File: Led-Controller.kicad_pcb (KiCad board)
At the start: 2 copper layers, 71.3 x 47.1 mm, 72 parts, among them J1 Program, J2 Barrel_Jack, J3 Screw_Terminal, Q1 CSD18540Q5B, Q2 CSD18540Q5B, Q3 CSD18540Q5B, Q4 CSD18540Q5B, Q5 CSD18540Q5B, Q6 CSD18540Q5B, U1 TPS5430DDA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

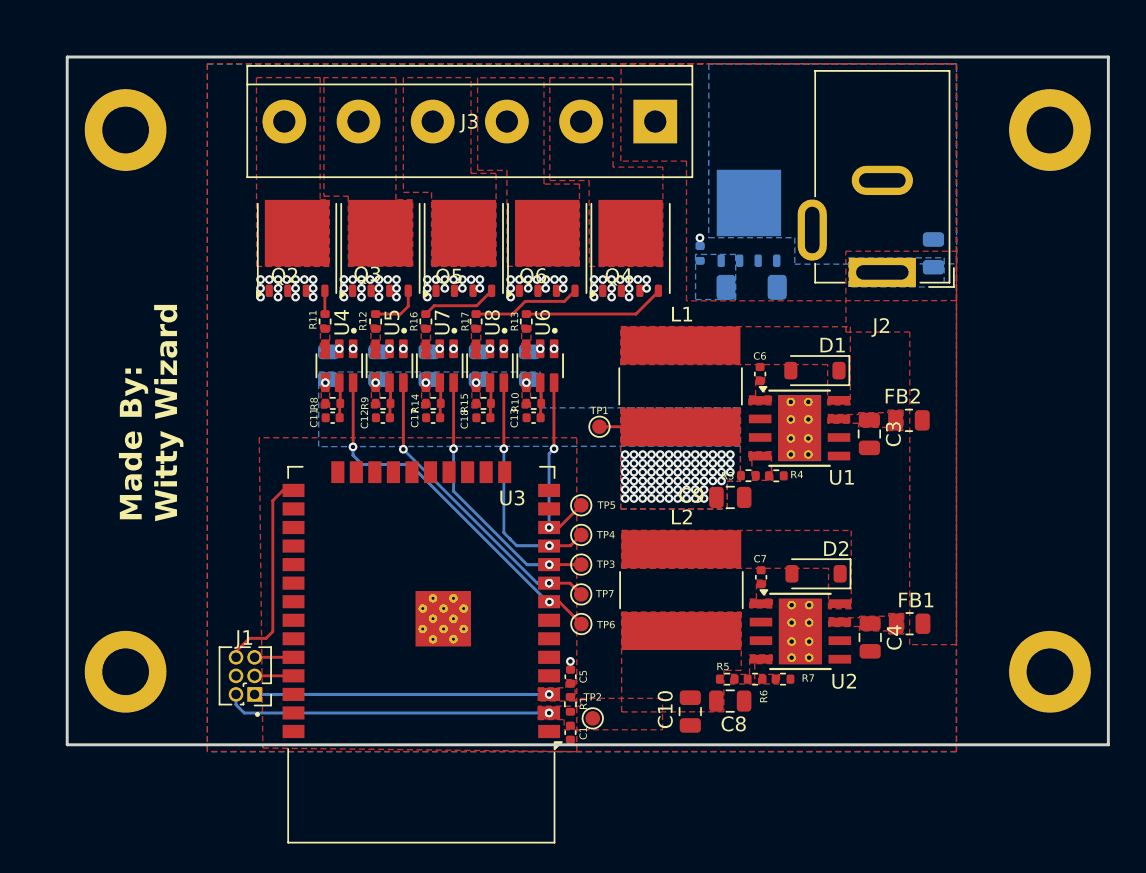
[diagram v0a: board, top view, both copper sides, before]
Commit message: Added: New power stage
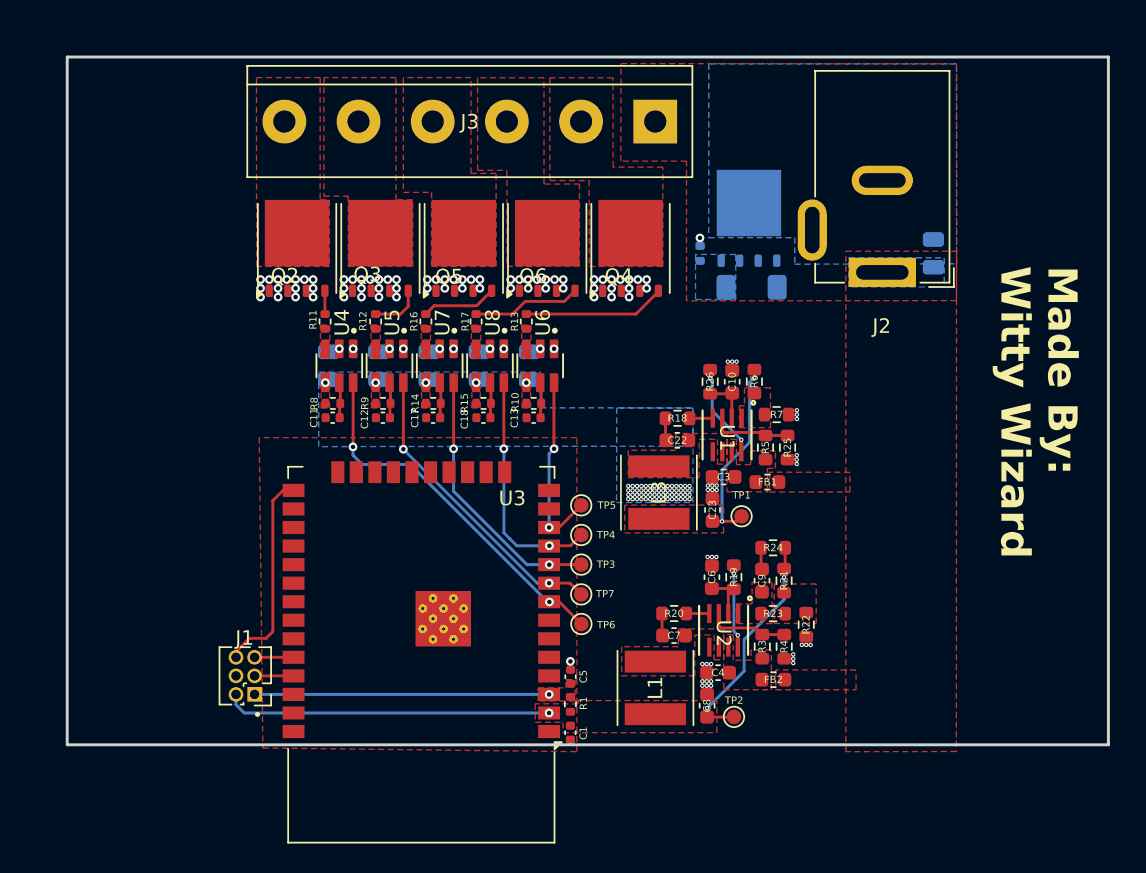
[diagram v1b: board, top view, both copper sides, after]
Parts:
- removed D1, D2: DSK34, Diode_SMD:D_SOD-123
- removed L2: 15uH, Inductor_SMD:L_Bourns-SRN8040_8x8.15mm
- removed REF** (x4): MountingHole_3.2mm_M3_DIN965_Pad, MountingHole:MountingHole_3.2mm_M3_DIN965_Pad
- added C22: 100n, Capacitor_SMD:C_0603_1608Metric, F.Cu at (145.7, 86.2)
- added C23: 33u, Capacitor_SMD:C_0603_1608Metric, F.Cu at (148.1, 91.0)
- added L3: 10u, Inductor_SMD:L_Taiyo-Yuden_MD-5050, F.Cu at (144.4, 89.8)
- added R18: 20, Resistor_SMD:R_0603_1608Metric, F.Cu at (145.7, 84.7)
- added R19: 100k, Resistor_SMD:R_0603_1608Metric, F.Cu at (149.6, 95.6)
- added R20: 20, Resistor_SMD:R_0603_1608Metric, F.Cu at (145.5, 98.1)
- added R21: 243k, Resistor_SMD:R_0603_1608Metric, F.Cu at (153.0, 95.8)
- added R22: 76.8k, Resistor_SMD:R_0603_1608Metric, F.Cu at (154.5, 98.8)
- added R23: 487, Resistor_SMD:R_0603_1608Metric, F.Cu at (152.2, 98.1)
- added R24: 243k, Resistor_SMD:R_0603_1608Metric, F.Cu at (152.2, 93.6)
- added R25: 21k, Resistor_SMD:R_0603_1608Metric, F.Cu at (153.2, 86.7)
- added R26: 100k, Resistor_SMD:R_0603_1608Metric, F.Cu at (147.9, 82.2)
- C10: value 22uf -> 100n; footprint Capacitor_SMD:C_0805_2012Metric -> Capacitor_SMD:C_0603_1608Metric
- C3, C4, C8: value 22uf -> 33u; footprint Capacitor_SMD:C_0805_2012Metric -> Capacitor_SMD:C_0603_1608Metric
- C6, C7: value 10nf -> 100n; footprint Capacitor_SMD:C_0402_1005Metric -> Capacitor_SMD:C_0603_1608Metric
- C9: value 22uf -> 33p; footprint Capacitor_SMD:C_0805_2012Metric -> Capacitor_SMD:C_0603_1608Metric
- FB1, FB2: value 220Ω -> 220; footprint Resistor_SMD:R_0805_2012Metric -> Inductor_SMD:L_0603_1608Metric
- L1: value 15uH -> 10u; footprint Inductor_SMD:L_Bourns-SRN8040_8x8.15mm -> Inductor_SMD:L_Taiyo-Yuden_MD-5050
- R3, R5: value 10kΩ -> 100k; footprint Resistor_SMD:R_0402_1005Metric -> Resistor_SMD:R_0603_1608Metric
- R4: value 1.5kΩ -> 21k; footprint Resistor_SMD:R_0402_1005Metric -> Resistor_SMD:R_0603_1608Metric
- R6: value 5.6kΩ -> 41.2k; footprint Resistor_SMD:R_0402_1005Metric -> Resistor_SMD:R_0603_1608Metric
- R7: value 270Ω -> 7.68k; footprint Resistor_SMD:R_0402_1005Metric -> Resistor_SMD:R_0603_1608Metric
- U1, U2: value TPS5430DDA -> MP9943AGQ-P; footprint Package_SO:TI_SO-PowerPAD-8_ThermalVias -> MP9943A:MP9943A
- moved C10 22.8 mm to (149.4, 82.2)
- moved L1 20.7 mm to (144.2, 103.2)
- moved R6 20.4 mm to (151.0, 82.2), turned to -90 degrees
- moved FB2 20.0 mm to (152.3, 102.6)
- moved R7 18.1 mm to (152.5, 84.4)
- moved R5 16.1 mm to (151.7, 86.7), turned to 90 degrees
- moved C6 14.3 mm to (148.1, 95.6)
- moved FB1 13.7 mm to (151.8, 89.1)
- moved R3 11.7 mm to (151.5, 100.3), turned to 90 degrees
- moved R4 11.7 mm to (153.0, 100.3), turned to -90 degrees
- moved TP1 11.5 mm to (150.1, 91.4)
- moved C4 10.7 mm to (148.5, 102.1), turned to 180 degrees
- moved C3 10.4 mm to (148.8, 88.7), turned to 180 degrees
- moved TP2 9.67 mm to (149.6, 105.1)
- moved C7 7.18 mm to (145.5, 99.6), turned to 0 degrees
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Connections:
- C10 pad 1: GND -> Net-(U1-VCC)
- C10 pad 2: +3.3V -> GND
- C3 pad 1: Net-(U1-VIN) -> Net-(U1-IN)
- C4 pad 1: Net-(U2-VIN) -> Net-(U2-IN)
- C6 pad 1: Net-(U1-BOOT) -> Net-(U2-VCC)
- C6 pad 2: Net-(D1-K) -> GND
- C7 pad 1: Net-(U2-BOOT) -> Net-(C7-Pad1)
- C7 pad 2: Net-(D2-K) -> Net-(U2-SW)
- C9 pad 1: GND -> Net-(U2-FB)
- C9 pad 2: +9V -> Net-(C9-Pad2)
- FB1 pad 2: Net-(U2-VIN) -> Net-(U1-IN)
- FB2 pad 2: Net-(U1-VIN) -> Net-(U2-IN)
- L1 pad 1: Net-(D1-K) -> Net-(U2-SW)
- L1 pad 2: +9V -> +3.3V
- R3 pad 1: +9V -> Net-(U2-IN)
- R3 pad 2: Net-(U1-VSENSE) -> Net-(U2-EN/SYNC)
- R4 pad 1: Net-(U1-VSENSE) -> Net-(U2-EN/SYNC)
- R5 pad 1: +3.3V -> Net-(U1-IN)
- R5 pad 2: Net-(U2-VSENSE) -> Net-(U1-EN/SYNC)
- R6 pad 1: Net-(U2-VSENSE) -> +9V
- R6 pad 2: Net-(R6-Pad2) -> Net-(U1-FB)
- R7 pad 1: Net-(R6-Pad2) -> Net-(U1-FB)
- U1 pad 1: Net-(U1-BOOT) -> Net-(U1-FB)
- U1 pad 2: unconnected-(U1-NC-Pad2) -> Net-(U1-VCC)
- U1 pad 3: unconnected-(U1-NC-Pad3) -> Net-(U1-EN/SYNC)
- U1 pad 4: Net-(U1-VSENSE) -> Net-(U1-BST)
- U1 pad 5: unconnected-(U1-EN-Pad5) -> GND
- U1 pad 6: GND -> Net-(U1-SW)
- U1 pad 7: Net-(U1-VIN) -> Net-(U1-IN)
- U1 pad 8: Net-(D1-K) -> Net-(U1-PG)
- U2 pad 1: Net-(U2-BOOT) -> Net-(U2-FB)
- U2 pad 2: unconnected-(U2-NC-Pad2) -> Net-(U2-VCC)
- U2 pad 3: unconnected-(U2-NC-Pad3) -> Net-(U2-EN/SYNC)
- U2 pad 4: Net-(U2-VSENSE) -> Net-(U2-BST)
- U2 pad 5: unconnected-(U2-EN-Pad5) -> GND
- U2 pad 6: GND -> Net-(U2-SW)
- U2 pad 7: Net-(U2-VIN) -> Net-(U2-IN)
- U2 pad 8: Net-(D2-K) -> Net-(U2-PG)
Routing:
- net +3.3V: track 22.5 -> 38.0 mm, vias 1 -> 3
- net +9V: track 5.57 -> 12.9 mm, vias 76 -> 67
- net Net-(U1-PG): track 0.00 -> 6.50 mm, vias 0 -> 2
- net Net-(U2-PG): track 0.00 -> 5.73 mm, vias 0 -> 2
- net Net-(U1-EN/SYNC): track 0.00 -> 5.69 mm
- net Net-(U2-EN/SYNC): track 0.00 -> 5.57 mm
- net Net-(U2-VCC): track 0.00 -> 3.62 mm
- net Net-(U1-VCC): track 0.00 -> 3.26 mm
- net Net-(U1-BST): track 0.00 -> 1.59 mm
- net Net-(U2-BST): track 0.00 -> 1.59 mm
- net Net-(C7-Pad1): track 0.00 -> 1.53 mm
- net Net-(C22-Pad1): track 0.00 -> 1.53 mm
- net Net-(C9-Pad2): track 0.00 -> 1.50 mm
- net GND: vias 79 -> 110
- added copper zone on F.Cu, net Net-(R21-Pad1)
- added copper zone on F.Cu, net Net-(U1-FB)
- added copper zone on F.Cu, net Net-(U1-IN)
- added copper zone on F.Cu, net Net-(U1-SW)
- added copper zone on F.Cu, net Net-(U2-FB)
- added copper zone on F.Cu, net Net-(U2-IN)
- added copper zone on F.Cu, net Net-(U2-SW)
- removed copper zone on F.Cu, net Net-(D1-K)
- removed copper zone on F.Cu, net Net-(D2-K)
- removed copper zone on F.Cu, net Net-(R6-Pad2)
- removed copper zone on F.Cu, net Net-(U1-BOOT)
- removed copper zone on F.Cu, net Net-(U1-VIN)
- removed copper zone on F.Cu, net Net-(U1-VSENSE)
- removed copper zone on F.Cu, net Net-(U2-BOOT)
- removed copper zone on F.Cu, net Net-(U2-VIN)
- removed copper zone on F.Cu, net Net-(U2-VSENSE)

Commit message: Added: new Inductor
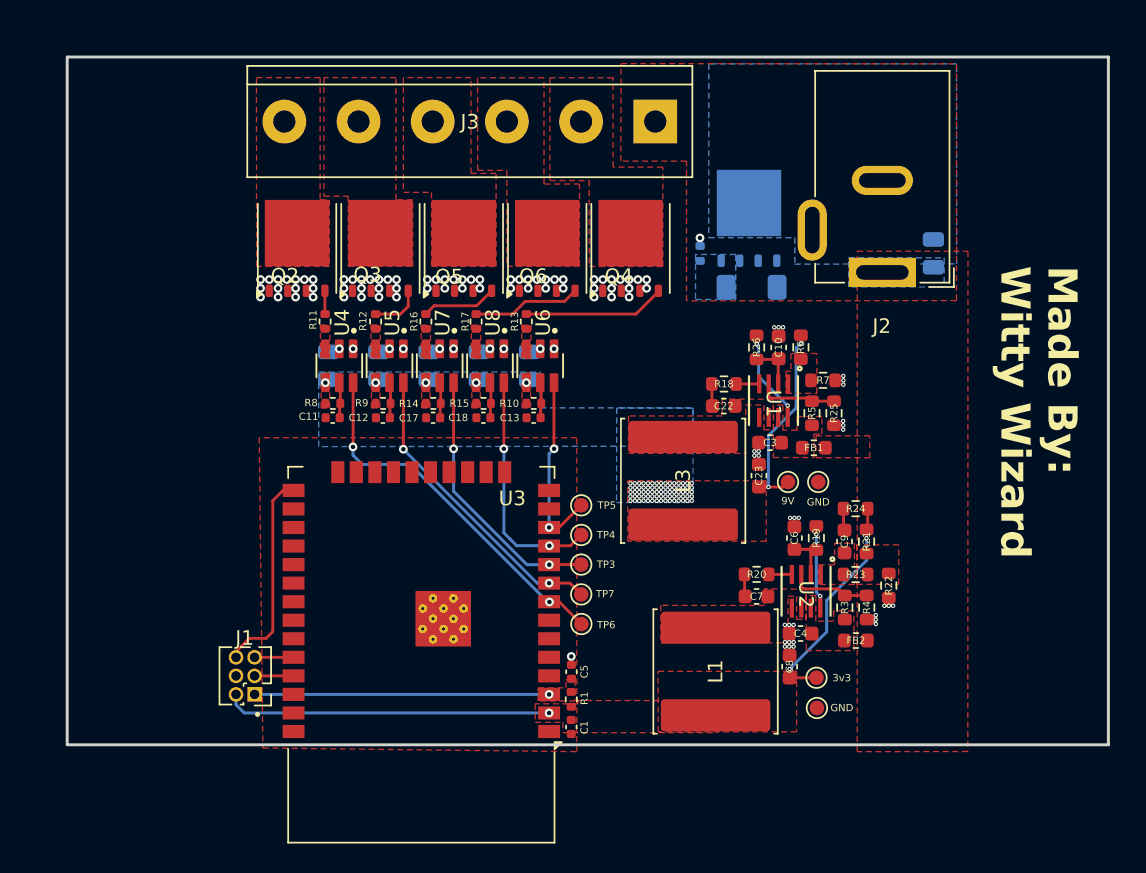
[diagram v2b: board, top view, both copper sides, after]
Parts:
- added GND: ~, TestPoint:TestPoint_Pad_D1.0mm, F.Cu at (155.2, 104.5)
- added GND: ~, TestPoint:TestPoint_Pad_D1.0mm, F.Cu at (155.3, 89.0)
- L1, L3: footprint Inductor_SMD:L_Taiyo-Yuden_MD-5050 -> Inductor_SMD:L_Changjiang_FNR8040S
- moved 3v3 6.25 mm to (155.2, 102.5)
- moved C8 6.25 mm to (153.4, 101.7)
- moved C9 6.25 mm to (157.1, 93.1)
- moved FB2 6.25 mm to (157.9, 99.9)
- moved R20 6.25 mm to (151.1, 95.4)
- moved R22 6.25 mm to (160.2, 96.1)
- moved C4 6.25 mm to (154.1, 99.4)
- moved R3 6.25 mm to (157.2, 97.7)
- moved R4 6.25 mm to (158.7, 97.7)
- moved U2 6.25 mm to (154.5, 96.5)
- moved R21 6.25 mm to (158.6, 93.1)
- moved R24 6.25 mm to (157.9, 90.9)
- moved C6 6.25 mm to (153.7, 92.9)
- moved C7 6.25 mm to (151.1, 96.9)
- moved R19 6.25 mm to (155.2, 92.9)
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- renumbered TP2 to 3v3, TP1 to 9V
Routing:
- net GND: track 0.03 -> 4.69 mm, vias 110 -> 108
- net +3.3V: track 38.0 -> 39.9 mm
- net +9V: vias 67 -> 82

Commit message: Minor fixes and layout changes
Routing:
- net +3.3V: track 39.9 -> 48.0 mm
- net +9V: track 12.9 -> 21.1 mm
- net GND: track 4.69 -> 0.35 mm
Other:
- board text added: "+VE"
- board text added: "CH1"
- board text added: "CH2"
- board text added: "CH3"
- board text added: "CH4"
- board text added: "CH5"
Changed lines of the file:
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@@
 		)
 		(property "Value" "Screw_Terminal"
-			(at 12.7 4.75 0)
+			(at 12.17 -0.04 0)
 			(layer "F.Fab")
 			(effects
@@
 		)
 		(property "Value" "Barrel_Jack"
-			(at 0 15.5 0)
+			(at -0.04 11.63 0)
 			(layer "F.Fab")
 			(effects
@@
 		)
 	)
-	(segment
-		(start 160.16 97.23)
-		(end 159.86 97.53)
-		(width 0.2)
-		(layer "F.Cu")
-		(net 1)
-	)
-	(segment
-		(start 160.16 97.23)
-		(end 160.46 97.53)
-		(width 0.2)
-		(layer "F.Cu")
-		(net 1)
-	)
-	(segment
-		(start 158.97 98.475)
-		(end 159.27 98.775)
-		(width 0.2)
-		(layer "F.Cu")
-		(net 1)
+	(gr_text "CH5\n"
+		(at 140.7 62.57 0)
+		(layer "B.SilkS")
+		(effects
+			(font
+				(size 1 1)
+				(thickness 0.25)
+				(bold yes)
+			)
+			(justify left bottom mirror)
+		)
 	)
-	(segment
-		(start 158.65 98.475)
-		(end 159.27 98.475)
-		(width 0.2)
-		(layer "F.Cu")
-		(net 1)
+	(gr_text "CH4\n"
+		(at 135.49 62.53 0)
+		(layer "B.SilkS")
+		(effects
+			(font
+				(size 1 1)
+				(thickness 0.25)
+				(bold yes)
+			)
+			(justify left bottom mirror)
+		)
 	)
-	(segment
-		(start 160.16 96.97)
-		(end 160.16 97.23)
-		(width 0.2)
-		(layer "F.Cu")
-		(net 1)
+	(gr_text "CH2"
+		(at 125.53 62.45 0)
+		(layer "B.SilkS")
+		(effects
+			(font
+				(size 1 1)
+				(thickness 0.25)
+				(bold yes)
+			)
+			(justify left bottom mirror)
+		)
 	)
-	(segment
-		(start 159.27 98.175)
-		(end 159.27 98.775)
-		(width 0.2)
-		(layer "F.Cu")
-		(net 1)
+	(gr_text "CH3\n"
+		(at 130.57 62.53 0)
+		(layer "B.SilkS")
+		(effects
+			(font
+				(size 1 1)
+				(thickness 0.25)
+				(bold yes)
+			)
+			(justify left bottom mirror)
+		)
 	)
-	(segment
-		(start 159.86 97.53)
-		(end 160.46 97.53)
-		(width 0.2)
-		(layer "F.Cu")
-		(net 1)
+	(gr_text "CH1\n"
+		(at 120.42 62.38 0)
+		(layer "B.SilkS")
+		(effects
+			(font
+				(size 1 1)
+				(thickness 0.25)
+				(bold yes)
+			)
+			(justify left bottom mirror)
+		)
 	)
-	(segment
-		(start 158.97 98.475)
-		(end 159.27 98.175)
-		(width 0.2)
-		(layer "F.Cu")
-		(net 1)
+	(gr_text "+VE"
+		(at 146.08 62.51 0)
+		(layer "B.SilkS")
+		(effects
+			(font
+				(size 1 1)
+				(thickness 0.25)
+				(bold yes)
+			)
+			(justify left bottom mirror)
+		)
 	)
 	(segment
@@
 	)
 	(segment
-		(start 160.16 96.97)
-		(end 160.16 97.53)
-		(width 0.2)
-		(layer "F.Cu")
-		(net 1)
-	)
-	(segment
 		(start 138.37 101.34)
 		(end 138.35 101.32)
@@
 	)
 	(segment
-		(start 155.91 97.16)
-		(end 155.91 99.32)
+		(start 161.4 101.59)
+		(end 161.13 101.86)
 		(width 0.2)
 		(layer "B.Cu")
@@
 	)
 	(segment
-		(start 158.64 92.9)
-		(end 158.64 94.43)
+		(start 161.13 101.86)
+		(end 153.37 101.86)
+		(width 0.2)
+		(layer "B.Cu")
+		(net 4)
+	)
+	(segment
+		(start 161.4 93.39)
+		(end 161.4 101.59)
 		(width 0.2)
 		(layer "B.Cu")
@@
 	)
 	(segment
-		(start 115.46 104.307106)
-		(end 116.022894 104.87)
+		(start 158.64 92.9)
+		(end 160.91 92.9)
 		(width 0.2)
 		(layer "B.Cu")
@@
 	)
 	(segment
-		(start 155.91 99.32)
-		(end 153.37 101.86)
+		(start 115.46 104.307106)
+		(end 116.022894 104.87)
 		(width 0.2)
 		(layer "B.Cu")
@@
 	)
 	(segment
-		(start 158.64 94.43)
-		(end 155.91 97.16)
+		(start 160.91 92.9)
+		(end 161.4 93.39)
 		(width 0.2)
 		(layer "B.Cu")
@@
 	)
 	(segment
-		(start 153.819998 83.98)
-		(end 151.919998 85.88)
+		(start 151.919998 89.4)
+		(end 157.48 89.4)
+		(width 0.2)
+		(layer "B.Cu")
+		(net 14)
+	)
+	(segment
+		(start 157.33 79.55)
+		(end 154.139998 79.55)
 		(width 0.2)
 		(layer "B.Cu")
@@
 	)
 	(segment
-		(start 153.819998 79.87)
-		(end 153.819998 83.98)
+		(start 157.8 80.02)
+		(end 157.33 79.55)
 		(width 0.2)
 		(layer "B.Cu")
@@
 	)
 	(segment
-		(start 154.139998 79.55)
-		(end 153.819998 79.87)
+		(start 157.48 89.4)
+		(end 157.8 89.08)
 		(width 0.2)
 		(layer "B.Cu")
@@
 	)
 	(segment
-		(start 151.919998 85.88)
-		(end 151.919998 89.4)
+		(start 157.8 89.08)
+		(end 157.8 80.02)
 		(width 0.2)
 		(layer "B.Cu")
@@
 		(polygon
 			(pts
-				(xy 141.83 60.4) (xy 164.8 60.42) (xy 164.8 76.63) (xy 146.31 76.65) (xy 146.31 67.08) (xy 141.81 67.08)
+				(xy 141.85 59.88) (xy 175.2 59.94) (xy 175.2 76.63) (xy 146.31 76.65) (xy 146.31 67.08) (xy 141.81 67.08)
+			)
+		)
+	)
+	(zone
+		(net 1)
+		(net_name "GND")
+		(layer "F.Cu")
+		(hatch edge 0.5)
+		(priority 24)
+		(connect_pads yes
+			(clearance 0.25)
+		)
+		(min_thickness 0.25)
+		(filled_areas_thickness no)
+		(fill yes
+			(thermal_gap 0.1)
+			(thermal_bridge_width 0.5)
+		)
+		(polygon
+			(pts
+				(xy 158.17 98.02) (xy 158.17 98.93) (xy 160.64 98.93) (xy 160.64 96.55) (xy 159.63 96.55) (xy 159.63 98.02)
 			)
 		)
@@
 		(polygon
 			(pts
-				(xy 142.28 88.97) (xy 151.77 88.97) (xy 151.77 93.11) (xy 142.29 93.11)
+				(xy 142.28 88.97) (xy 146.81 88.98) (xy 146.82 90.58) (xy 150.57 90.58) (xy 150.57 88.97) (xy 151.77 88.97)
+				(xy 151.77 93.11) (xy 142.29 93.11)
 			)
 		)
@@
 		(polygon
 			(pts
-				(xy 165.583222 73.249738) (xy 165.573222 107.509738) (xy 158.003222 107.519738) (xy 158.003222 73.249738)
+				(xy 175.23 73.25) (xy 175.21 107.05) (xy 158.01 107.05) (xy 158.003222 73.249738)
 			)
 		)
@@
 		(priority 1)
 		(connect_pads
-			(clearance 0.5)
+			(clearance 0.25)
 		)
 		(min_thickness 0.25)
@@
 		(fill yes
 			(thermal_gap 0.1)
-			(thermal_bridge_width 0.7)
+			(thermal_bridge_width 0.5)
 		)
 		(polygon

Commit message: Fixed DFM Issues
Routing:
- net +9V: vias 82 -> 37

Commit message: review pending
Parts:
- removed 3v3, 9V, GND (x2): ~, TestPoint:TestPoint_Pad_D1.0mm
- added C21: 470uf, Capacitor_THT:CP_Radial_D10.0mm_P2.50mm_P5.00mm, F.Cu at (164.2, 82.0)
- added C24: 470uf, Capacitor_THT:CP_Radial_D10.0mm_P2.50mm_P5.00mm, F.Cu at (166.9, 94.1)
- added C25: 100nf, Capacitor_SMD:C_0402_1005Metric, B.Cu at (108.0, 80.9)
- added C26: 100nf, Capacitor_SMD:C_0402_1005Metric, B.Cu at (111.5, 80.9)
- added C27: 100nf, Capacitor_SMD:C_0402_1005Metric, B.Cu at (114.9, 80.9)
- added C28: 100nf, Capacitor_SMD:C_0402_1005Metric, B.Cu at (118.4, 80.9)
- added C29: 100nf, Capacitor_SMD:C_0402_1005Metric, B.Cu at (121.8, 80.9)
- added C30: 100nf, Capacitor_SMD:C_0402_1005Metric, F.Cu at (134.0, 77.4)
- added C31: 22uf, Capacitor_SMD:C_0805_2012Metric, F.Cu at (135.8, 77.6)
- added C32: 100nf, Capacitor_SMD:C_0402_1005Metric, B.Cu at (106.7, 70.8)
- added C33: 100nf, Capacitor_SMD:C_0402_1005Metric, B.Cu at (111.7, 70.8)
- added C34: 100nf, Capacitor_SMD:C_0402_1005Metric, B.Cu at (116.7, 70.8)
- added C35: 100nf, Capacitor_SMD:C_0402_1005Metric, B.Cu at (121.9, 70.5)
- added C36: 100nf, Capacitor_SMD:C_0402_1005Metric, B.Cu at (127.1, 70.4)
- added J4: Screw_Terminal, TerminalBlock:TerminalBlock_bornier-2_P5.08mm, F.Cu at (167.5, 64.5)
- added J5: Ws2812 Conn, Connector_PinHeader_2.54mm:PinHeader_1x03_P2.54mm_Horizontal, F.Cu at (136.8, 70.7)
- added J6: Screw_Terminal, TerminalBlock:TerminalBlock_bornier-2_P5.08mm, F.Cu at (146.4, 64.2)
- added JP1: Jumper_3_Open, Jumper:SolderJumper-3_P2.0mm_Open_TrianglePad1.0x1.5mm, F.Cu at (143.7, 82.9)
- added R27: 100, Resistor_SMD:R_0402_1005Metric, B.Cu at (106.7, 67.9)
- added R28: 100, Resistor_SMD:R_0402_1005Metric, B.Cu at (111.8, 67.9)
- added R29: 100, Resistor_SMD:R_0402_1005Metric, B.Cu at (116.8, 67.8)
- added R30: 100, Resistor_SMD:R_0402_1005Metric, B.Cu at (121.9, 67.6)
- added R31: 100, Resistor_SMD:R_0402_1005Metric, B.Cu at (127.1, 67.3)
- added R33: 37.4k, Resistor_SMD:R_0603_1608Metric, F.Cu at (155.8, 79.9)
- added TP1: ~, TestPoint:TestPoint_Pad_D1.0mm, F.Cu at (142.7, 98.7)
- added TP2: ~, TestPoint:TestPoint_Pad_D1.0mm, F.Cu at (160.0, 104.2)
- added TP8: ~, TestPoint:TestPoint_Pad_D1.0mm, F.Cu at (115.1, 92.2)
- added U9: SN74LV1T34DBV, Package_TO_SOT_SMD:SOT-23-5, F.Cu at (139.2, 77.6)
- J1: footprint Connector_PinHeader_1.27mm:PinHeader_2x03_P1.27mm_Vertical -> Connector_PinHeader_2.54mm:PinHeader_2x03_P2.54mm_Vertical
- moved C13 12.0 mm to (123.8, 84.3)
- moved C14 12.0 mm to (116.6, 80.7)
- moved C17 12.0 mm to (116.9, 84.3)
- moved C18 12.0 mm to (120.4, 84.3)
- moved C19 12.0 mm to (120.1, 80.7)
- moved C20 12.0 mm to (123.5, 80.7)
- moved Q5 12.0 mm to (119.0, 72.7)
- moved Q6 12.0 mm to (124.7, 72.7)
- moved R11 12.0 mm to (109.5, 77.7)
- moved R13 12.0 mm to (123.3, 77.7)
- moved R16 12.0 mm to (116.4, 77.7)
- moved R17 12.0 mm to (119.9, 77.7)
- moved R8 12.0 mm to (110.1, 83.3)
- moved R9 12.0 mm to (113.5, 83.3)
- moved U4 12.0 mm to (110.5, 80.7)
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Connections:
- U3 pad 27: unconnected-(U3-IO16-Pad27) -> /DOUT
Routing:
- net /DOUT: track 0.00 -> 53.5 mm, vias 0 -> 2
- net Net-(JP1-C): track 0.00 -> 18.0 mm
- net +5V: track 0.00 -> 13.8 mm
- net /IN5: track 12.9 -> 25.4 mm
- net /IN3: track 18.3 -> 30.7 mm
- net /IN2: track 20.9 -> 33.3 mm
- net /IN4: track 16.3 -> 28.5 mm
- net /IN1: track 25.5 -> 36.1 mm
- net +3.3V: track 48.0 -> 55.4 mm
- net +9V: track 21.1 -> 27.7 mm, vias 37 -> 42
- net Net-(J5-Pin_2): track 0.00 -> 6.17 mm
- net Net-(U1-FB): track 0.00 -> 5.02 mm
- net /OUT1: track 0.00 -> 3.46 mm
- net /OUT2: track 0.00 -> 3.40 mm
- net /OUT3: track 0.00 -> 3.32 mm
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- removed copper zone on F.Cu, net Net-(U1-FB)
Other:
- board size 71.3 x 47.1 mm -> 74.3 x 47.4 mm
- board text added: "Made By: Ansh Chawla Original Design by: Witty Wizard"
- board text removed: "Made By: Witty Wizard"
